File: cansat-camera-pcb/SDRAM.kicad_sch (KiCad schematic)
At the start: 10 parts

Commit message: -4g modul(4g modul on other pcb)
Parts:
- removed U5: ~, symbol cansat-camera-pcb-symbols:IS42S16800F-5TLI
- added U1: IS42S16800F-5TLI, symbol gaia-camera-symbols:IS42S16800F-5TLI
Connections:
- net +3.3V: now also U1.1 (VDD), U1.14 (VDD), U1.27 (VDD), U1.3 (VDDQ), U1.43 (VDDQ), U1.49 (VDDQ), U1.9 (VDDQ)
- net A0: now also U1.23 (A0)
- net A1: now also U1.24 (A1)
- net A10: now also U1.22 (A10)
- net A11: now also U1.35 (A11)
- net A2: now also U1.25 (A2)
- net A3: now also U1.26 (A3)
- net A4: now also U1.29 (A4)
- net A5: now also U1.30 (A5)
- net A6: now also U1.31 (A6)
- net A7: now also U1.32 (A7)
- net A8: now also U1.33 (A8)
- net A9: now also U1.34 (A9)
- net BA0: now also U1.20 (BA0)
- net BA1: now also U1.21 (BA1)
- net CAS: now also U1.17 (CAS)
- net CKE: now also U1.37 (CKE)
- net CLK: now also U1.38 (CLK)
- net CS: now also U1.19 (CS)
- net DQ0: now also U1.2 (DQ0)
- net DQ1: now also U1.4 (DQ9)
- net DQ10: now also U1.45 (DQ10)
- net DQ11: now also U1.47 (DQ11)
- net DQ12: now also U1.48 (DQ12)
- net DQ13: now also U1.50 (DQ13)
- net DQ14: now also U1.51 (DQ14)
- net DQ15: now also U1.53 (DQ15)
- net DQ2: now also U1.5 (DQ2)
- net DQ3: now also U1.7 (DQ3)
- net DQ4: now also U1.8 (DQ4)
- net DQ5: now also U1.10 (DQ5)
- net DQ6: now also U1.11 (DQ6)
- net DQ7: now also U1.13 (DQ7)
- net DQ8: now also U1.42 (DQ8)
- net DQ9: now also U1.4 (DQ9)
- net DQMH: now also U1.39 (DQMH)
- net DQML: now also U1.15 (DQML)
- net GND: now also U1.12 (VSSQ), U1.28 (VSS), U1.41 (VSS), U1.46 (VSSQ), U1.52 (VSSQ), U1.54 (VSS), U1.6 (VSSQ)
- net RAS: now also U1.18 (RAS)
- net WE: now also U1.16 (WE)
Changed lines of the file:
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@@
+	)
+	(symbol
+		(lib_id "gaia-camera-symbols:IS42S16800F-5TLI")
+		(at 140.97 22.86 0)
+		(unit 1)
+		(exclude_from_sim no)
+		(in_bom yes)
+		(on_board yes)
+		(dnp no)
+		(fields_autoplaced yes)
+		(property "Reference" "U1"
+			(at 147.955 17.78 0)
+			(effects
+				(font
+					(size 1.27 1.27)
+				)
+			)
+		)
+		(property "Value" "IS42S16800F-5TLI"
+			(at 147.955 20.32 0)
+			(effects
+				(font
+					(size 1.27 1.27)
+				)
+			)
+		)
+		(property "Footprint" ""
+			(at 140.97 22.86 0)
+			(effects
+				(font
+					(size 1.27 1.27)
+				)
+				(hide yes)
+			)
+		)
+		(property "Datasheet" ""
+			(at 140.97 22.86 0)
+			(effects
+				(font
+					(size 1.27 1.27)
+				)
+				(hide yes)
+			)
+		)
+		(property "Description" ""
+			(at 140.97 22.86 0)
+			(effects
+				(font
+					(size 1.27 1.27)
+				)
+				(hide yes)
+			)
+		)
+		(pin "6"
+		)
+		(pin "9"
+		)
+		(pin "1"
+		)
+		(pin "2"
+		)
+		(pin "3"
+		)
+		(pin "4"
+		)
+		(pin "5"
+		)
+		(pin "7"
+		)
+		(pin "8"
+		)
+		(pin "12"
+		)
+		(pin "19"
+		)
+		(pin "50"
+		)
+		(pin "20"
+		)
+		(pin "17"
+		)
+		(pin "23"
+		)
+		(pin "11"
+		)
+		(pin "25"
+		)
+		(pin "16"
+		)
+		(pin "15"
+		)
+		(pin "14"
+		)
+		(pin "52"
+		)
+		(pin "26"
+		)
+		(pin "27"
+		)
+		(pin "51"
+		)
+		(pin "42"
+		)
+		(pin "39"
+		)
+		(pin "41"
+		)
+		(pin "21"
+		)
+		(pin "38"
+		)
+		(pin "13"
+		)
+		(pin "22"
+		)
+		(pin "54"
+		)
+		(pin "53"
+		)
+		(pin "10"
+		)
+		(pin "18"
+		)
+		(pin "24"
+		)
+		(pin "48"
+		)
+		(pin "49"
+		)
+		(pin "47"
+		)
+		(pin "46"
+		)
+		(pin "45"
+		)
+		(pin "4"
+		)
+		(pin "43"
+		)
+		(pin "40"
+		)
+		(pin "30"
+		)
+		(pin "37"
+		)
+		(pin "34"
+		)
+		(pin "33"
+		)
+		(pin "36"
+		)
+		(pin "29"
+		)
+		(pin "35"
+		)
+		(pin "31"
+		)
+		(pin "32"
+		)
+		(pin "28"
+		)
+		(instances
+			(project ""
+				(path "/ff55e53a-9379-43eb-9b08-9bace1f81889/12f64f3d-24be-4094-a17a-c73af9bffac2"
+					(reference "U1")
+					(unit 1)
+				)
+			)
+		)
 	)
 	(symbol
@@
 					(unit 1)
 				)
-			)
-		)
-	)
-	(symbol
-		(lib_id "cansat-camera-pcb-symbols:IS42S16800F-5TLI")
-		(at 140.97 22.86 0)
-		(unit 1)
-		(exclude_from_sim no)
-		(in_bom yes)
-		(on_board yes)
-		(dnp no)
-		(property "Reference" "U5"
-			(at 147.828 21.59 0)
-			(effects
-				(font
-					(size 1.27 1.27)
-				)
-			)
-		)
-		(property "Value" "~"
-			(at 147.955 21.59 0)
-			(effects
-				(font
-					(size 1.27 1.27)
-				)
-			)
-		)
-		(property "Footprint" ""
-			(at 140.97 22.86 0)
-			(effects
-				(font
-					(size 1.27 1.27)
-				)
-				(hide yes)
-			)
-		)
-		(property "Datasheet" ""
-			(at 140.97 22.86 0)
-			(effects
-				(font
-					(size 1.27 1.27)
-				)
-				(hide yes)
-			)
-		)
-		(property "Description" ""
-			(at 140.97 22.86 0)
-			(effects
-				(font
-					(size 1.27 1.27)
-				)
-				(hide yes)
-			)
-		)
-		(pin "16"
-		)
-		(pin "8"
-		)
-		(pin "9"
-		)
-		(pin "10"
-		)
-		(pin "11"
-		)
-		(pin "13"
-		)
-		(pin "12"
-		)
-		(pin "14"
-		)
-		(pin "15"
-		)
-		(pin "4"
-		)
-		(pin "46"
-		)
-		(pin "50"
-		)
-		(pin "48"
-		)
-		(pin "20"
-		)
-		(pin "52"
-		)
-		(pin "49"
-		)
-		(pin "34"
-		)
-		(pin "41"
-		)
-		(pin "37"
-		)
-		(pin "47"
-		)
-		(pin "21"
-		)
-		(pin "25"
-		)
-		(pin "51"
-		)
-		(pin "17"
-		)
-		(pin "23"
-		)
-		(pin "24"
-		)
-		(pin "22"
-		)
-		(pin "18"
-		)
-		(pin "19"
-		)
-		(pin "27"
-		)
-		(pin "54"
-		)
-		(pin "53"
-		)
-		(pin "26"
-		)
-		(pin "45"
-		)
-		(pin "43"
-		)
-		(pin "42"
-		)
-		(pin "40"
-		)
-		(pin "39"
-		)
-		(pin "38"
-		)
-		(pin "36"
-		)
-		(pin "35"
-		)
-		(pin "33"
-		)
-		(pin "32"
-		)
-		(pin "31"
-		)
-		(pin "30"
-		)
-		(pin "28"
-		)
-		(pin "29"
-		)
-		(pin "5"
-		)
-		(pin "6"
-		)
-		(pin "7"
-		)
-		(pin "4"
-		)
-		(pin "1"
-		)
-		(pin "3"
-		)
-		(pin "2"
-		)
-		(instances
-			(project "cansat-camera-pcb"
-				(path "/ff55e53a-9379-43eb-9b08-9bace1f81889/12f64f3d-24be-4094-a17a-c73af9bffac2"
-					(reference "U5")
-					(unit 1)
-				)

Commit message: Footprint assign
Reset kivételével minden hozzácsatolva
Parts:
- C25, C26, C27, C29, C30, C31, C32: footprint (none) -> Capacitor_SMD:C_0402_1005Metric
- C28, C33: footprint (none) -> Capacitor_SMD:C_0201_0603Metric
- U1: footprint (none) -> gaia-camera-footprints:IS42S16800F-5TLI
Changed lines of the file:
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@@
 			)
 		)
-		(property "Footprint" ""
+		(property "Footprint" "Capacitor_SMD:C_0402_1005Metric"
 			(at 46.99 33.02 0)
 			(effects
@@
 			)
 		)
-		(property "Footprint" ""
+		(property "Footprint" "gaia-camera-footprints:IS42S16800F-5TLI"
 			(at 140.97 22.86 0)
 			(effects
@@
 			)
 		)
-		(property "Footprint" ""
+		(property "Footprint" "Capacitor_SMD:C_0402_1005Metric"
 			(at 46.99 101.6 0)
 			(effects
@@
 			)
 		)
-		(property "Footprint" ""
+		(property "Footprint" "Capacitor_SMD:C_0402_1005Metric"
 			(at 46.99 44.45 0)
 			(effects
@@
 			)
 		)
-		(property "Footprint" ""
+		(property "Footprint" "Capacitor_SMD:C_0201_0603Metric"
 			(at 46.99 113.03 0)
 			(effects
@@
 			)
 		)
-		(property "Footprint" ""
+		(property "Footprint" "Capacitor_SMD:C_0402_1005Metric"
 			(at 46.99 55.88 0)
 			(effects
@@
 			)
 		)
-		(property "Footprint" ""
+		(property "Footprint" "Capacitor_SMD:C_0402_1005Metric"
 			(at 46.99 90.17 0)
 			(effects
@@
 			)
 		)
-		(property "Footprint" ""
+		(property "Footprint" "Capacitor_SMD:C_0402_1005Metric"
 			(at 46.99 67.31 0)
 			(effects
@@
 			)
 		)
-		(property "Footprint" ""
+		(property "Footprint" "Capacitor_SMD:C_0201_0603Metric"
 			(at 46.99 124.46 0)
 			(effects
@@
 			)
 		)
-		(property "Footprint" ""
+		(property "Footprint" "Capacitor_SMD:C_0402_1005Metric"
 			(at 46.99 78.74 0)
 			(effects

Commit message: Footprint assign final
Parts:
- C28, C33: footprint Capacitor_SMD:C_0201_0603Metric -> Capacitor_SMD:C_0603_1608Metric
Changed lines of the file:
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@@
 			)
 		)
-		(property "Footprint" "Capacitor_SMD:C_0201_0603Metric"
+		(property "Footprint" "Capacitor_SMD:C_0603_1608Metric"
 			(at 46.99 113.03 0)
 			(effects
@@
 			)
 		)
-		(property "Footprint" "Capacitor_SMD:C_0201_0603Metric"
+		(property "Footprint" "Capacitor_SMD:C_0603_1608Metric"
 			(at 46.99 124.46 0)
 			(effects

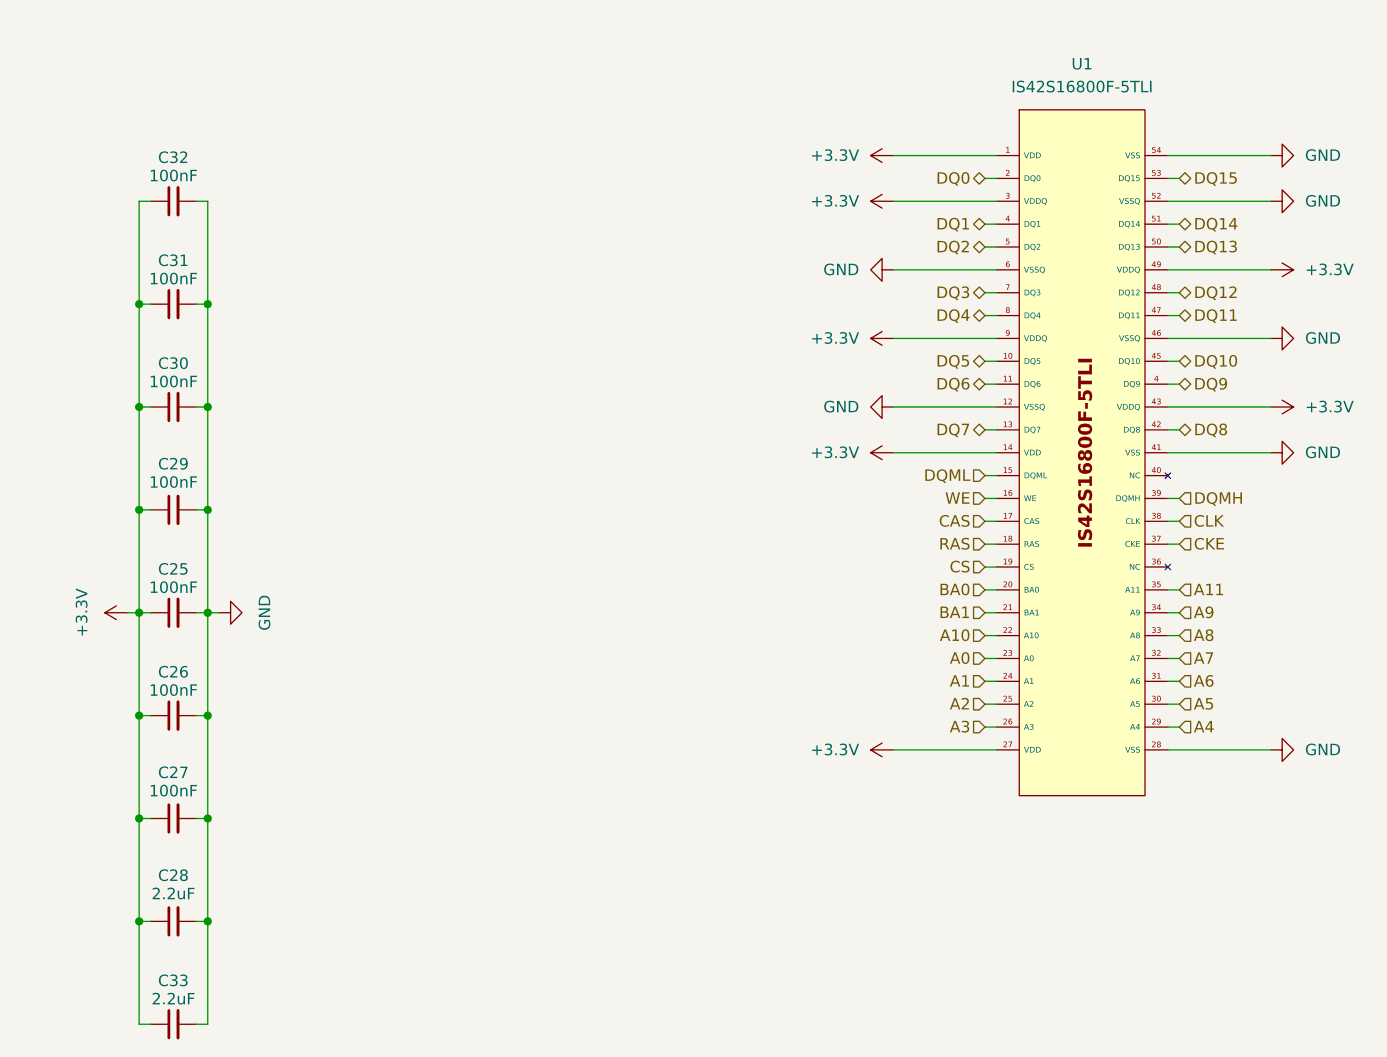
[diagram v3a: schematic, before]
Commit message: Routing+SDram csere
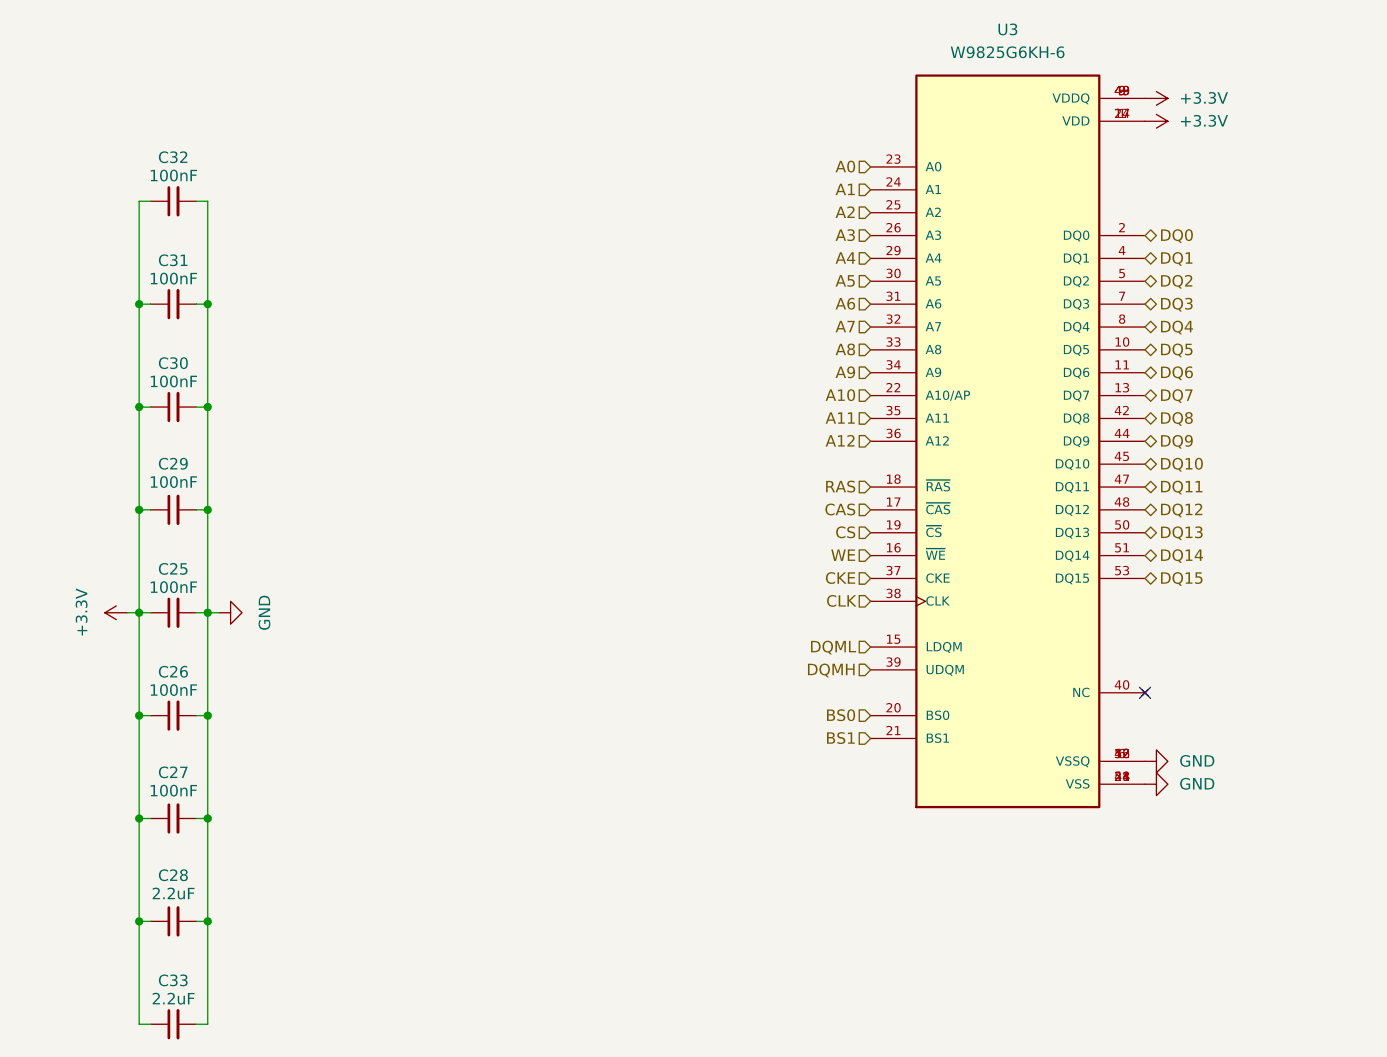
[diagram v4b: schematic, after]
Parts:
- removed U1: IS42S16800F-5TLI, gaia-camera-footprints:IS42S16800F-5TLI, symbol gaia-camera-symbols:IS42S16800F-5TLI
- added U3: W9825G6KH-6, Package_SO:TSOP-II-54_22.2x10.16mm_P0.8mm, symbol gaia-camera-symbols:W9825G6KH-6
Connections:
- net +3.3V: now also U3.1 (VDD), U3.14 (VDD), U3.27 (VDD), U3.3 (VDDQ), U3.43 (VDDQ), U3.49 (VDDQ), U3.9 (VDDQ)
- net A0: now also U3.23 (A0)
- net A1: now also U3.24 (A1)
- net A10: now also U3.22 (A10/AP)
- net A11: now also U3.35 (A11)
- net A2: now also U3.25 (A2)
- net A3: now also U3.26 (A3)
- net A4: now also U3.29 (A4)
- net A5: now also U3.30 (A5)
- net A6: now also U3.31 (A6)
- net A7: now also U3.32 (A7)
- net A8: now also U3.33 (A8)
- net A9: now also U3.34 (A9)
- net CAS: now also U3.17 (~{CAS})
- net CKE: now also U3.37 (CKE)
- net CLK: now also U3.38 (CLK)
- net CS: now also U3.19 (~{CS})
- net DQ0: now also U3.2 (DQ0)
- net DQ1: now also U3.4 (DQ1)
- net DQ10: now also U3.45 (DQ10)
- net DQ11: now also U3.47 (DQ11)
- net DQ12: now also U3.48 (DQ12)
- net DQ13: now also U3.50 (DQ13)
- net DQ14: now also U3.51 (DQ14)
- net DQ15: now also U3.53 (DQ15)
- net DQ2: now also U3.5 (DQ2)
- net DQ3: now also U3.7 (DQ3)
- net DQ4: now also U3.8 (DQ4)
- net DQ5: now also U3.10 (DQ5)
- net DQ6: now also U3.11 (DQ6)
- net DQ7: now also U3.13 (DQ7)
- net DQ8: now also U3.42 (DQ8)
- net DQ9: now also U3.44 (DQ9)
- net DQMH: now also U3.39 (UDQM)
- net DQML: now also U3.15 (LDQM)
- net GND: now also U3.12 (VSSQ), U3.28 (VSS), U3.41 (VSS), U3.46 (VSSQ), U3.52 (VSSQ), U3.54 (VSS), U3.6 (VSSQ)
- net RAS: now also U3.18 (~{RAS})
- net WE: now also U3.16 (~{WE})
- new net A12: U3.36 (A12)
- new net BS0: U3.20 (BS0)
- new net BS1: U3.21 (BS1)
- no-connect marks 0 -> 1

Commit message: Routolás sdram
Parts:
- removed U3: W9825G6KH-6, Package_SO:TSOP-II-54_22.2x10.16mm_P0.8mm, symbol gaia-camera-symbols:W9825G6KH-6
- added IC1: W9825G6JB-6I, Package_BGA:Alliance_TFBGA-54_8x8mm_Layout9x9_P0.8mm, symbol gaia-camera-symbols:W9825G6JB-6I
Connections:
- net +3.3V: now also IC1.A7 (VDDQ_1), IC1.A9 (VDD_1), IC1.B3 (VDDQ_2), IC1.C7 (VDDQ_3), IC1.D3 (VDDQ_4), IC1.E7 (VDD_2), IC1.J9 (VDD_3)
- net A0: now also IC1.H7 (A0)
- net A1: now also IC1.H8 (A1)
- net A10: now also IC1.H9 (A10)
- net A11: now also IC1.G2 (A11)
- net A12: now also IC1.G1 (A12)
- net A2: now also IC1.J8 (A2)
- net A3: now also IC1.J7 (A3)
- net A4: now also IC1.J3 (A4)
- net A5: now also IC1.J2 (A5)
- net A6: now also IC1.H3 (A6)
- net A7: now also IC1.H2 (A7)
- net A8: now also IC1.H1 (A8)
- net A9: now also IC1.G3 (A9)
- net BS0: now also IC1.G7 (BS0)
- net BS1: now also IC1.G8 (BS1)
- net CAS: now also IC1.F7 (~{CAS})
- net CKE: now also IC1.F3 (CKE)
- net CLK: now also IC1.F2 (CLK)
- net CS: now also IC1.G9 (~{CS})
- net DQ0: now also IC1.A8 (DQ0)
- net DQ1: now also IC1.B9 (DQ1)
- net DQ10: now also IC1.D1 (DQ10)
- net DQ11: now also IC1.C2 (DQ11)
- net DQ12: now also IC1.C1 (DQ12)
- net DQ13: now also IC1.B2 (DQ13)
- net DQ14: now also IC1.B1 (DQ14)
- net DQ15: now also IC1.A2 (DQ15)
- net DQ2: now also IC1.B8 (DQ2)
- net DQ3: now also IC1.C9 (DQ3)
- net DQ4: now also IC1.C8 (DQ4)
- net DQ5: now also IC1.D9 (DQ5)
- net DQ6: now also IC1.D8 (DQ6)
- net DQ7: now also IC1.E9 (DQ7)
- net DQ8: now also IC1.E1 (DQ8)
- net DQ9: now also IC1.D2 (DQ9)
- net DQMH: now also IC1.F1 (UDQM)
- net DQML: now also IC1.E8 (LDQM)
- net GND: now also IC1.A1 (VSS_1), IC1.A3 (VSSQ_1), IC1.B7 (VSSQ_2), IC1.C3 (VSSQ_3), IC1.D7 (VSSQ_4), IC1.E3 (VSS_2), IC1.J1 (VSS_3)
- net RAS: now also IC1.F8 (~{RAS})
- net WE: now also IC1.F9 (~{WE})

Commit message: Regulator+
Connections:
- net +3.3V renamed +3.3VA

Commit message: send to production
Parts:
- IC1: footprint Package_BGA:Alliance_TFBGA-54_8x8mm_Layout9x9_P0.8mm -> gaia-camera-footprints:Alliance_TFBGA-54_8x8mm_Layout9x9_P0.8mm
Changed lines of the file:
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@@
 			)
 		)
-		(property "Footprint" "Package_BGA:Alliance_TFBGA-54_8x8mm_Layout9x9_P0.8mm"
+		(property "Footprint" "gaia-camera-footprints:Alliance_TFBGA-54_8x8mm_Layout9x9_P0.8mm"
 			(at 106.68 122.86 0)
 			(effects

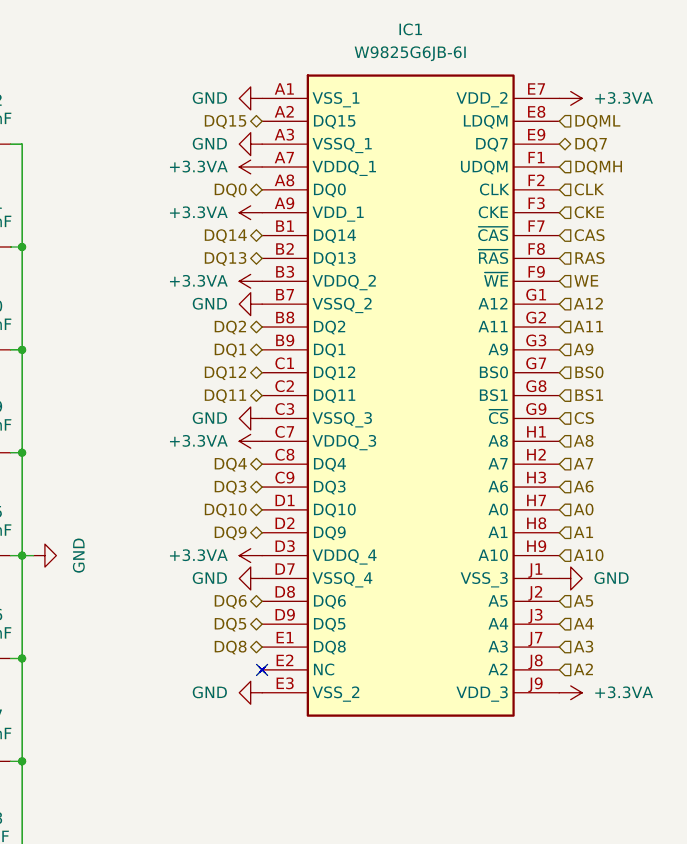
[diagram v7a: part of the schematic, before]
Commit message: Sdram reroute
Nem több mint a cím
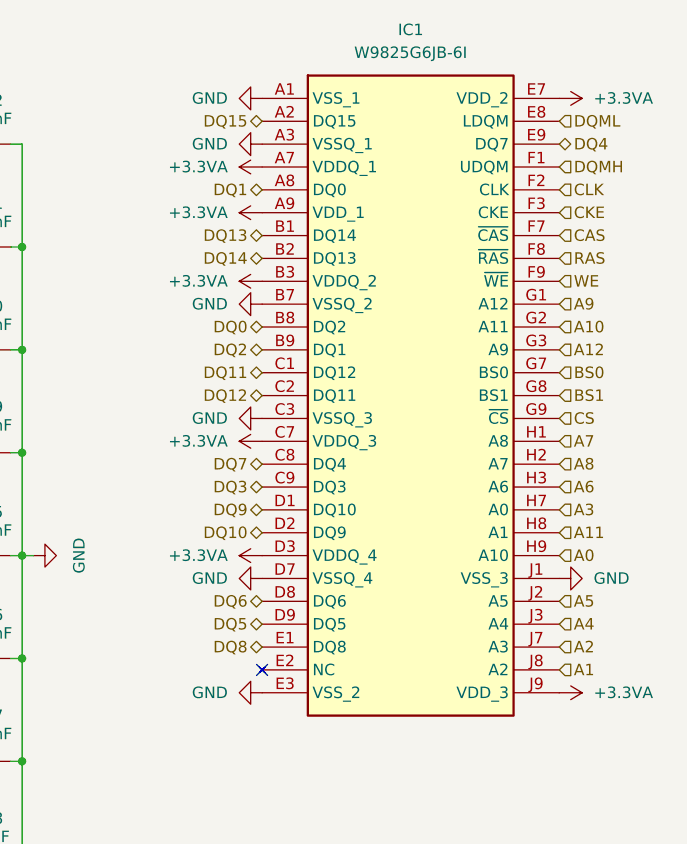
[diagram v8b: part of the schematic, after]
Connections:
- net A0: now also IC1.H9 (A10); no longer IC1.H7 (A0)
- net A1: now also IC1.J8 (A2); no longer IC1.H8 (A1)
- net A10: now also IC1.G2 (A11); no longer IC1.H9 (A10)
- net A11: now also IC1.H8 (A1); no longer IC1.G2 (A11)
- net A12: now also IC1.G3 (A9); no longer IC1.G1 (A12)
- net A2: now also IC1.J7 (A3); no longer IC1.J8 (A2)
- net A3: now also IC1.H7 (A0); no longer IC1.J7 (A3)
- net A7: now also IC1.H1 (A8); no longer IC1.H2 (A7)
- net A8: now also IC1.H2 (A7); no longer IC1.H1 (A8)
- net A9: now also IC1.G1 (A12); no longer IC1.G3 (A9)
- net DQ0: now also IC1.B8 (DQ2); no longer IC1.A8 (DQ0)
- net DQ1: now also IC1.A8 (DQ0); no longer IC1.B9 (DQ1)
- net DQ10: now also IC1.D2 (DQ9); no longer IC1.D1 (DQ10)
- net DQ11: now also IC1.C1 (DQ12); no longer IC1.C2 (DQ11)
- net DQ12: now also IC1.C2 (DQ11); no longer IC1.C1 (DQ12)
- net DQ13: now also IC1.B1 (DQ14); no longer IC1.B2 (DQ13)
- net DQ14: now also IC1.B2 (DQ13); no longer IC1.B1 (DQ14)
- net DQ2: now also IC1.B9 (DQ1); no longer IC1.B8 (DQ2)
- net DQ4: now also IC1.E9 (DQ7); no longer IC1.C8 (DQ4)
- net DQ7: now also IC1.C8 (DQ4); no longer IC1.E9 (DQ7)
- net DQ9: now also IC1.D1 (DQ10); no longer IC1.D2 (DQ9)
